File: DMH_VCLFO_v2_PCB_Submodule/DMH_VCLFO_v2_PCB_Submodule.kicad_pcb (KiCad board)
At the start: 2 copper layers, 88 x 70 mm, 3 parts, among them J41 Conn_02x03_Odd_Even, J43 Conn_02x03_Odd_Even, J45 Conn_02x03_Odd_Even

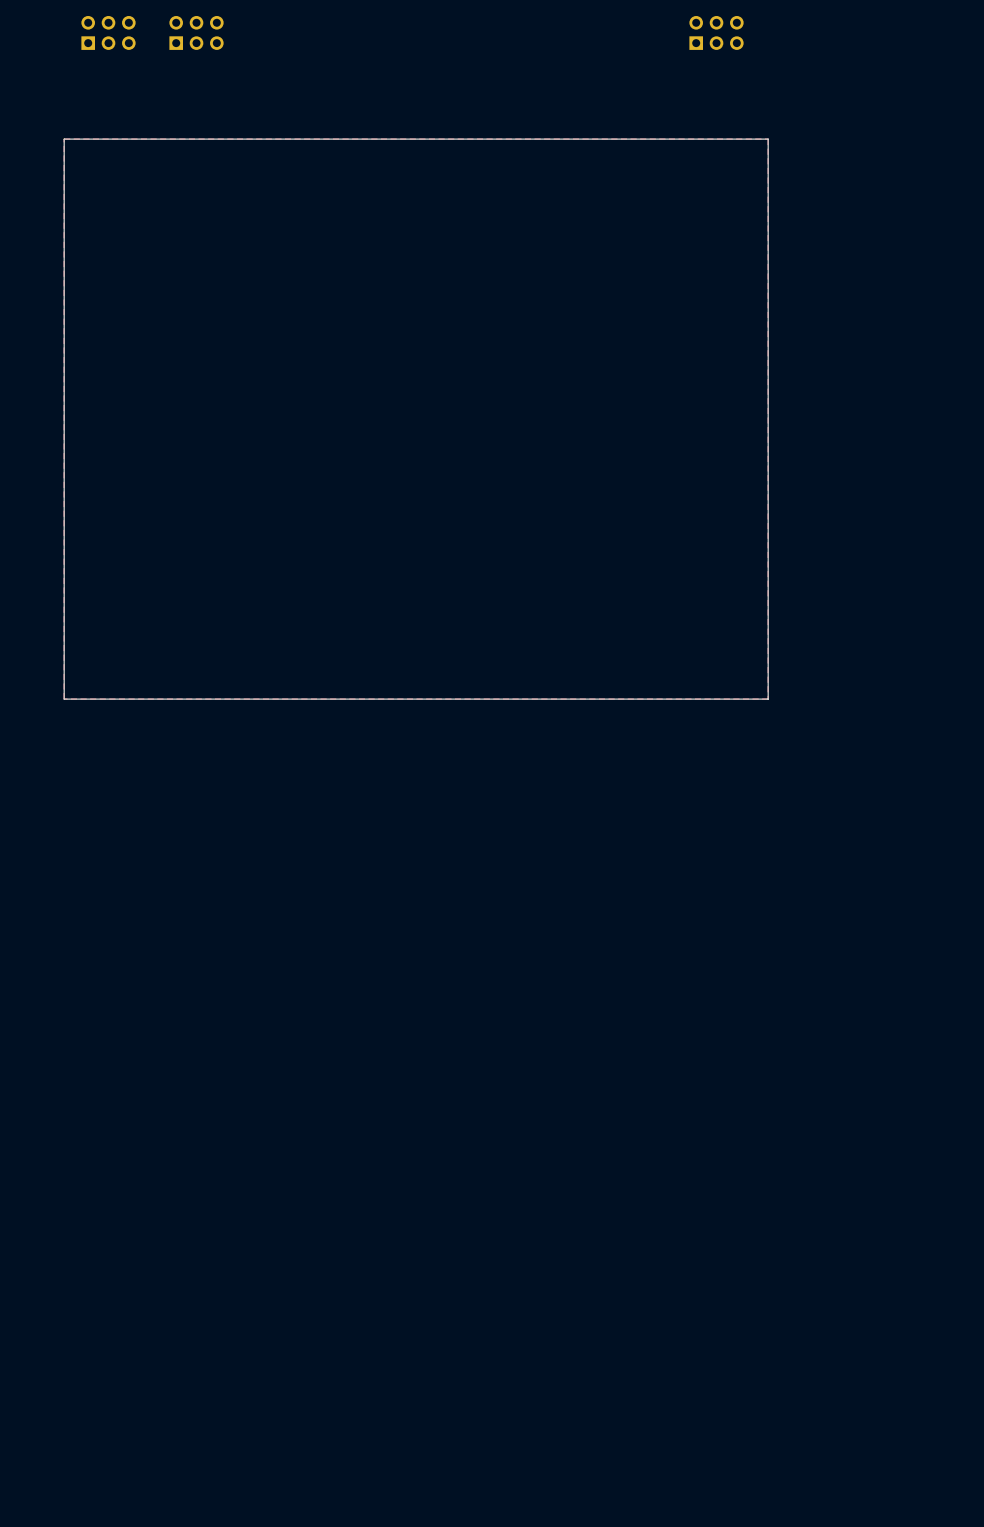
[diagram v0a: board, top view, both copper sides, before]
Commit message: Submodule comp placement started
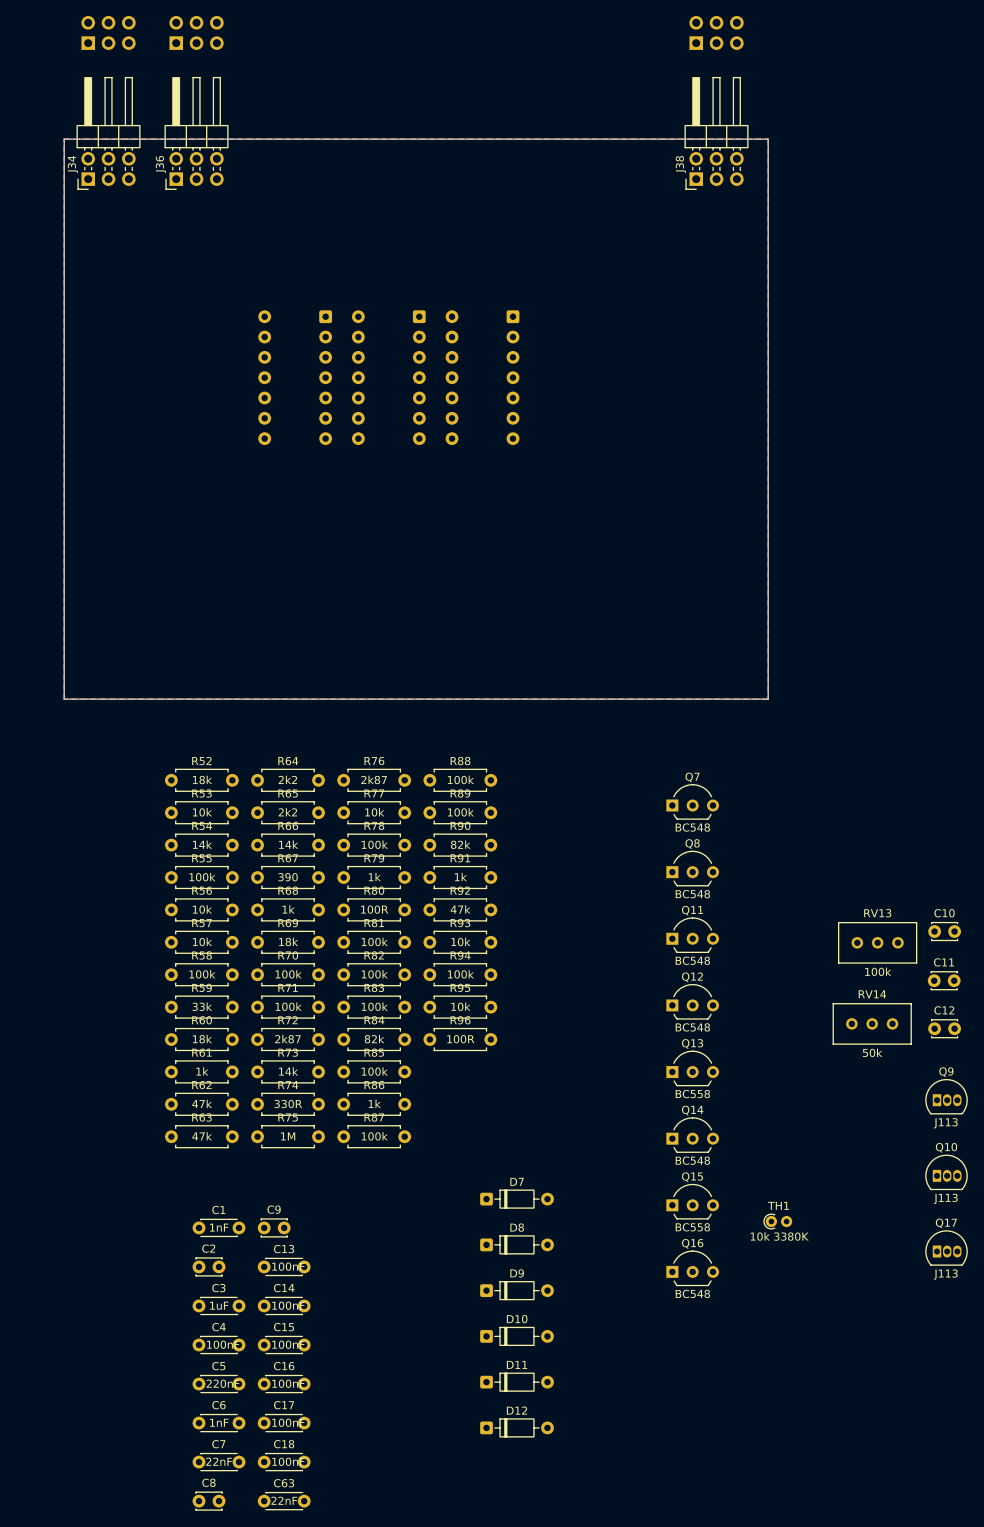
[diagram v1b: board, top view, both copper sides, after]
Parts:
- removed J41, J43, J45: Conn_02x03_Odd_Even, Connector_PinSocket_2.54mm:PinSocket_2x03_P2.54mm_Vertical
- added C1: 1nF, Capacitor_THT:C_Disc_D4.3mm_W1.9mm_P5.00mm, F.Cu at (72.8, 166.1)
- added C10: 10pF, Capacitor_THT:C_Disc_D3.0mm_W2.0mm_P2.50mm, F.Cu at (164.8, 129.1)
- added C11: 10pF, Capacitor_THT:C_Disc_D3.0mm_W2.0mm_P2.50mm, F.Cu at (164.8, 135.2)
- added C12: 100pF, Capacitor_THT:C_Disc_D3.0mm_W2.0mm_P2.50mm, F.Cu at (164.8, 141.2)
- added C13: 100nF, Capacitor_THT:C_Disc_D4.3mm_W1.9mm_P5.00mm, F.Cu at (81.0, 171.0)
- added C14: 100nF, Capacitor_THT:C_Disc_D4.3mm_W1.9mm_P5.00mm, F.Cu at (81.0, 175.9)
- added C15: 100nF, Capacitor_THT:C_Disc_D4.3mm_W1.9mm_P5.00mm, F.Cu at (81.0, 180.7)
- added C16: 100nF, Capacitor_THT:C_Disc_D4.3mm_W1.9mm_P5.00mm, F.Cu at (81.0, 185.6)
- added C17: 100nF, Capacitor_THT:C_Disc_D4.3mm_W1.9mm_P5.00mm, F.Cu at (81.0, 190.5)
- added C18: 100nF, Capacitor_THT:C_Disc_D4.3mm_W1.9mm_P5.00mm, F.Cu at (81.0, 195.4)
- added C2: 100pF, Capacitor_THT:C_Disc_D3.0mm_W2.0mm_P2.50mm, F.Cu at (72.8, 171.0)
- added C3: 1uF, Capacitor_THT:C_Disc_D4.3mm_W1.9mm_P5.00mm, F.Cu at (72.8, 175.9)
- added C4: 100nF, Capacitor_THT:C_Disc_D4.3mm_W1.9mm_P5.00mm, F.Cu at (72.8, 180.7)
- added C5: 220nF, Capacitor_THT:C_Disc_D4.3mm_W1.9mm_P5.00mm, F.Cu at (72.8, 185.6)
- added C6: 1nF, Capacitor_THT:C_Disc_D4.3mm_W1.9mm_P5.00mm, F.Cu at (72.8, 190.5)
- added C63: 22nF, Capacitor_THT:C_Disc_D4.3mm_W1.9mm_P5.00mm, F.Cu at (81.0, 200.2)
- added C7: 22nF, Capacitor_THT:C_Disc_D4.3mm_W1.9mm_P5.00mm, F.Cu at (72.8, 195.4)
- added C8: 100pF, Capacitor_THT:C_Disc_D3.0mm_W2.0mm_P2.50mm, F.Cu at (72.8, 200.2)
- added C9: 2.2nF, Capacitor_THT:C_Disc_D3.0mm_W2.0mm_P2.50mm, F.Cu at (81.0, 166.1)
- added D10: 1N4148, Diode_THT:D_DO-35_SOD27_P7.62mm_Horizontal, F.Cu at (108.8, 179.7)
- added D11: 1N4148, Diode_THT:D_DO-35_SOD27_P7.62mm_Horizontal, F.Cu at (108.8, 185.4)
- added D12: 1N4148, Diode_THT:D_DO-35_SOD27_P7.62mm_Horizontal, F.Cu at (108.8, 191.1)
- added D7: 1N4148, Diode_THT:D_DO-35_SOD27_P7.62mm_Horizontal, F.Cu at (108.8, 162.5)
- added D8: 1N4148, Diode_THT:D_DO-35_SOD27_P7.62mm_Horizontal, F.Cu at (108.8, 168.2)
- added D9: 1N4148, Diode_THT:D_DO-35_SOD27_P7.62mm_Horizontal, F.Cu at (108.8, 173.9)
- added J34: Conn_02x03_Odd_Even, Connector_PinHeader_2.54mm:PinHeader_2x03_P2.54mm_Horizontal, F.Cu at (59.0, 35.0)
- added J35: Conn_02x03_Odd_Even, Connector_PinSocket_2.54mm:PinSocket_2x03_P2.54mm_Vertical, B.Cu at (59.0, 18.0)
- added J36: Conn_02x03_Odd_Even, Connector_PinHeader_2.54mm:PinHeader_2x03_P2.54mm_Horizontal, F.Cu at (70.0, 35.0)
- added J37: Conn_02x03_Odd_Even, Connector_PinSocket_2.54mm:PinSocket_2x03_P2.54mm_Vertical, B.Cu at (70.0, 18.0)
- added J38: Conn_02x03_Odd_Even, Connector_PinHeader_2.54mm:PinHeader_2x03_P2.54mm_Horizontal, F.Cu at (135.0, 35.0)
- added J39: Conn_02x03_Odd_Even, Connector_PinSocket_2.54mm:PinSocket_2x03_P2.54mm_Vertical, B.Cu at (135.0, 18.0)
- added Q10: J113, Package_TO_SOT_THT:TO-92L_Inline, F.Cu at (165.1, 159.6)
- added Q11: BC548, Package_TO_SOT_THT:TO-92L_Inline_Wide, F.Cu at (132.0, 130.0)
- added Q12: BC548, Package_TO_SOT_THT:TO-92L_Inline_Wide, F.Cu at (132.0, 138.3)
- added Q13: BC558, Package_TO_SOT_THT:TO-92L_Inline_Wide, F.Cu at (132.0, 146.6)
- added Q14: BC548, Package_TO_SOT_THT:TO-92L_Inline_Wide, F.Cu at (132.0, 154.9)
- added Q15: BC558, Package_TO_SOT_THT:TO-92L_Inline_Wide, F.Cu at (132.0, 163.3)
- added Q16: BC548, Package_TO_SOT_THT:TO-92L_Inline_Wide, F.Cu at (132.0, 171.6)
- added Q17: J113, Package_TO_SOT_THT:TO-92L_Inline, F.Cu at (165.1, 169.1)
- added Q7: BC548, Package_TO_SOT_THT:TO-92L_Inline_Wide, F.Cu at (132.0, 113.3)
- added Q8: BC548, Package_TO_SOT_THT:TO-92L_Inline_Wide, F.Cu at (132.0, 121.6)
- added Q9: J113, Package_TO_SOT_THT:TO-92L_Inline, F.Cu at (165.1, 150.1)
- added R52: 18k, Resistor_THT:R_Axial_DIN0207_L6.3mm_D2.5mm_P7.62mm_Horizontal, F.Cu at (69.4, 110.2)
- added R53: 10k, Resistor_THT:R_Axial_DIN0207_L6.3mm_D2.5mm_P7.62mm_Horizontal, F.Cu at (69.4, 114.2)
- added R54: 14k, Resistor_THT:R_Axial_DIN0207_L6.3mm_D2.5mm_P7.62mm_Horizontal, F.Cu at (69.4, 118.2)
- added R55: 100k, Resistor_THT:R_Axial_DIN0207_L6.3mm_D2.5mm_P7.62mm_Horizontal, F.Cu at (69.4, 122.3)
- added R56: 10k, Resistor_THT:R_Axial_DIN0207_L6.3mm_D2.5mm_P7.62mm_Horizontal, F.Cu at (69.4, 126.3)
- added R57: 10k, Resistor_THT:R_Axial_DIN0207_L6.3mm_D2.5mm_P7.62mm_Horizontal, F.Cu at (69.4, 130.4)
- added R58: 100k, Resistor_THT:R_Axial_DIN0207_L6.3mm_D2.5mm_P7.62mm_Horizontal, F.Cu at (69.4, 134.4)
- added R59: 33k, Resistor_THT:R_Axial_DIN0207_L6.3mm_D2.5mm_P7.62mm_Horizontal, F.Cu at (69.4, 138.5)
- added R60: 18k, Resistor_THT:R_Axial_DIN0207_L6.3mm_D2.5mm_P7.62mm_Horizontal, F.Cu at (69.4, 142.6)
- added R61: 1k, Resistor_THT:R_Axial_DIN0207_L6.3mm_D2.5mm_P7.62mm_Horizontal, F.Cu at (69.4, 146.6)
- added R62: 47k, Resistor_THT:R_Axial_DIN0207_L6.3mm_D2.5mm_P7.62mm_Horizontal, F.Cu at (69.4, 150.7)
- added R63: 47k, Resistor_THT:R_Axial_DIN0207_L6.3mm_D2.5mm_P7.62mm_Horizontal, F.Cu at (69.4, 154.7)
- added R64: 2k2, Resistor_THT:R_Axial_DIN0207_L6.3mm_D2.5mm_P7.62mm_Horizontal, F.Cu at (80.2, 110.2)
- added R65: 2k2, Resistor_THT:R_Axial_DIN0207_L6.3mm_D2.5mm_P7.62mm_Horizontal, F.Cu at (80.2, 114.2)
- added R66: 14k, Resistor_THT:R_Axial_DIN0207_L6.3mm_D2.5mm_P7.62mm_Horizontal, F.Cu at (80.2, 118.2)
- added R67: 390, Resistor_THT:R_Axial_DIN0207_L6.3mm_D2.5mm_P7.62mm_Horizontal, F.Cu at (80.2, 122.3)
- added R68: 1k, Resistor_THT:R_Axial_DIN0207_L6.3mm_D2.5mm_P7.62mm_Horizontal, F.Cu at (80.2, 126.3)
- added R69: 18k, Resistor_THT:R_Axial_DIN0207_L6.3mm_D2.5mm_P7.62mm_Horizontal, F.Cu at (80.2, 130.4)
- added R70: 100k, Resistor_THT:R_Axial_DIN0207_L6.3mm_D2.5mm_P7.62mm_Horizontal, F.Cu at (80.2, 134.4)
- added R71: 100k, Resistor_THT:R_Axial_DIN0207_L6.3mm_D2.5mm_P7.62mm_Horizontal, F.Cu at (80.2, 138.5)
- added R72: 2k87, Resistor_THT:R_Axial_DIN0207_L6.3mm_D2.5mm_P7.62mm_Horizontal, F.Cu at (80.2, 142.6)
- added R73: 14k, Resistor_THT:R_Axial_DIN0207_L6.3mm_D2.5mm_P7.62mm_Horizontal, F.Cu at (80.2, 146.6)
- added R74: 330R, Resistor_THT:R_Axial_DIN0207_L6.3mm_D2.5mm_P7.62mm_Horizontal, F.Cu at (80.2, 150.7)
- added R75: 1M, Resistor_THT:R_Axial_DIN0207_L6.3mm_D2.5mm_P7.62mm_Horizontal, F.Cu at (80.2, 154.7)
- added R76: 2k87, Resistor_THT:R_Axial_DIN0207_L6.3mm_D2.5mm_P7.62mm_Horizontal, F.Cu at (90.9, 110.2)
- added R77: 10k, Resistor_THT:R_Axial_DIN0207_L6.3mm_D2.5mm_P7.62mm_Horizontal, F.Cu at (90.9, 114.2)
- added R78: 100k, Resistor_THT:R_Axial_DIN0207_L6.3mm_D2.5mm_P7.62mm_Horizontal, F.Cu at (90.9, 118.2)
- added R79: 1k, Resistor_THT:R_Axial_DIN0207_L6.3mm_D2.5mm_P7.62mm_Horizontal, F.Cu at (90.9, 122.3)
- added R80: 100R, Resistor_THT:R_Axial_DIN0207_L6.3mm_D2.5mm_P7.62mm_Horizontal, F.Cu at (90.9, 126.3)
- added R81: 100k, Resistor_THT:R_Axial_DIN0207_L6.3mm_D2.5mm_P7.62mm_Horizontal, F.Cu at (90.9, 130.4)
- added R82: 100k, Resistor_THT:R_Axial_DIN0207_L6.3mm_D2.5mm_P7.62mm_Horizontal, F.Cu at (90.9, 134.4)
- added R83: 100k, Resistor_THT:R_Axial_DIN0207_L6.3mm_D2.5mm_P7.62mm_Horizontal, F.Cu at (90.9, 138.5)
- added R84: 82k, Resistor_THT:R_Axial_DIN0207_L6.3mm_D2.5mm_P7.62mm_Horizontal, F.Cu at (90.9, 142.6)
- added R85: 100k, Resistor_THT:R_Axial_DIN0207_L6.3mm_D2.5mm_P7.62mm_Horizontal, F.Cu at (90.9, 146.6)
- added R86: 1k, Resistor_THT:R_Axial_DIN0207_L6.3mm_D2.5mm_P7.62mm_Horizontal, F.Cu at (90.9, 150.7)
- added R87: 100k, Resistor_THT:R_Axial_DIN0207_L6.3mm_D2.5mm_P7.62mm_Horizontal, F.Cu at (90.9, 154.7)
- added R88: 100k, Resistor_THT:R_Axial_DIN0207_L6.3mm_D2.5mm_P7.62mm_Horizontal, F.Cu at (101.7, 110.2)
- added R89: 100k, Resistor_THT:R_Axial_DIN0207_L6.3mm_D2.5mm_P7.62mm_Horizontal, F.Cu at (101.7, 114.2)
- added R90: 82k, Resistor_THT:R_Axial_DIN0207_L6.3mm_D2.5mm_P7.62mm_Horizontal, F.Cu at (101.7, 118.2)
- added R91: 1k, Resistor_THT:R_Axial_DIN0207_L6.3mm_D2.5mm_P7.62mm_Horizontal, F.Cu at (101.7, 122.3)
- added R92: 47k, Resistor_THT:R_Axial_DIN0207_L6.3mm_D2.5mm_P7.62mm_Horizontal, F.Cu at (101.7, 126.3)
- added R93: 10k, Resistor_THT:R_Axial_DIN0207_L6.3mm_D2.5mm_P7.62mm_Horizontal, F.Cu at (101.7, 130.4)
- added R94: 100k, Resistor_THT:R_Axial_DIN0207_L6.3mm_D2.5mm_P7.62mm_Horizontal, F.Cu at (101.7, 134.4)
- added R95: 10k, Resistor_THT:R_Axial_DIN0207_L6.3mm_D2.5mm_P7.62mm_Horizontal, F.Cu at (101.7, 138.5)
- added R96: 100R, Resistor_THT:R_Axial_DIN0207_L6.3mm_D2.5mm_P7.62mm_Horizontal, F.Cu at (101.7, 142.6)
- added RV13: 100k, Potentiometer_THT:Potentiometer_Bourns_3296W_Vertical, F.Cu at (160.2, 130.5)
- added RV14: 50k, Potentiometer_THT:Potentiometer_Bourns_3296W_Vertical, F.Cu at (159.5, 140.6)
- added TH1: 10k 3380K, Resistor_THT:R_Axial_DIN0204_L3.6mm_D1.6mm_P1.90mm_Vertical, F.Cu at (144.4, 165.3)
- added U10: TL074, Package_DIP:DIP-14_W7.62mm_Socket, B.Cu at (88.7, 52.2)
- added U11: TL074, Package_DIP:DIP-14_W7.62mm_Socket, B.Cu at (100.4, 52.2)
- added U12: TL074, Package_DIP:DIP-14_W7.62mm_Socket, B.Cu at (112.1, 52.2)

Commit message: Submodule com placement done
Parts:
- removed J35, J37, J39: Conn_02x03_Odd_Even, Connector_PinSocket_2.54mm:PinSocket_2x03_P2.54mm_Vertical
- C1, C10, C11, C12, C13, C14, C15, C16, C17, C18, C2, C3, C4, C5, C6, C63, C7, C8, C9, D10, D11, D12, D7, D8, D9, Q10, Q11, Q12, Q13, Q14, Q15, Q16, Q17, Q7, Q8, Q9, R52, R53, R54, R55, R56, R57, R58, R59, R60, R61, R62, R63, R64, R65, R66, R67, R68, R69, R70, R71, R72, R73, R74, R75, R76, R77, R78, R79, R80, R81, R82, R83, R84, R85, R86, R87, R88, R89, R90, R91, R92, R93, R94, R95, R96, RV13, RV14: moved to B.Cu
- TH1: value 10k 3380K -> 10k3380; moved to B.Cu
- moved Q10 160.3 mm to (56.3, 41.9)
- moved C63 158.2 mm to (65.6, 42.8)
- moved C7 149.4 mm to (65.6, 46.1)
- moved C5 146.3 mm to (65.6, 39.5)
- moved D12 139.4 mm to (93.2, 52.6), turned to 180 degrees
- moved C6 138.2 mm to (123.9, 62.1), turned to 180 degrees
- moved C15 137.0 mm to (129.4, 52.6)
- moved C1 134.5 mm to (97.5, 33.9)
- moved C2 134.3 mm to (111.8, 42.5)
- moved Q17 130.0 mm to (78.7, 71.9), turned to -90 degrees
- moved TH1 129.9 mm to (54.5, 71.5), turned to 180 degrees
- moved C18 128.3 mm to (129.5, 76.6)
- moved C8 124.8 mm to (92.3, 77.0)
- moved C14 124.4 mm to (97.5, 52.6)
- moved C4 124.1 mm to (146.8, 81.1), turned to 90 degrees
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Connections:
- C3 pad 2: Net-(U12A-+) -> Net-(U12D-+)
- C6 pad 1: Net-(U12D-+) -> Net-(U12A-+)
- R71 pad 2: Net-(U12A--) -> Net-(U12D--)
- R73 pad 1: Net-(U12A-+) -> Net-(U12D-+)
- R74 pad 1: Net-(U12A--) -> Net-(U12D--)
- R78 pad 1: Net-(U12D-+) -> Net-(U12A-+)
- U12 pad 1: Net-(Q9-D) -> Net-(D10-K)
- U12 pad 10: Net-(Q8-C) -> Net-(Q9-S)
- U12 pad 13: /SubModule A/Comp_Ref -> Net-(U12D--)
- U12 pad 14: Net-(D10-K) -> Net-(Q9-D)
- U12 pad 2: Net-(U12A--) -> /SubModule A/Comp_Ref
- U12 pad 5: Net-(Q9-S) -> Net-(Q8-C)
- U12 pad 6: A_Rnd_S -> Net-(Q7-C)
- U12 pad 7: A_Rnd_S -> Net-(R54-Pad2)
- U12 pad 8: Net-(R54-Pad2) -> A_Rnd_S
- U12 pad 9: Net-(Q7-C) -> A_Rnd_S
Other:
- board size 88 x 70 mm -> 100 x 70 mm

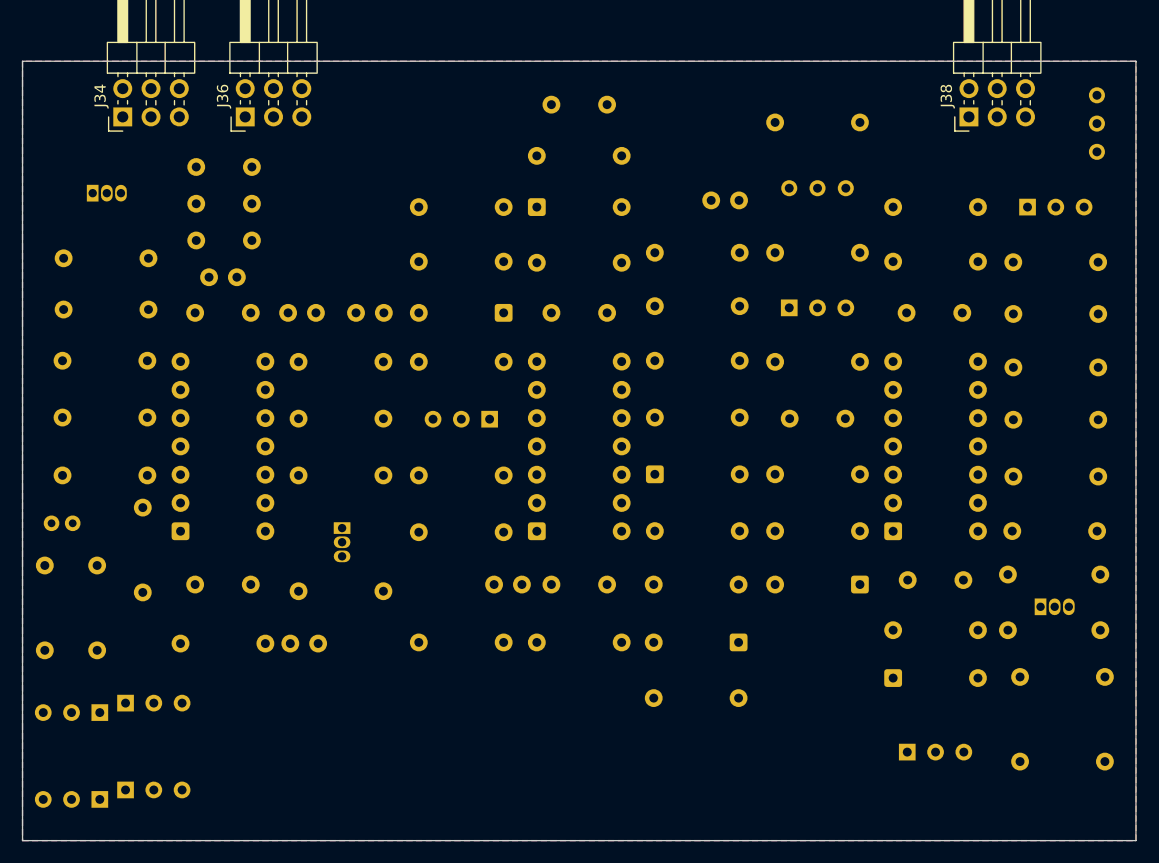
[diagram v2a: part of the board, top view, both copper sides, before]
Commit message: Submodule routing done
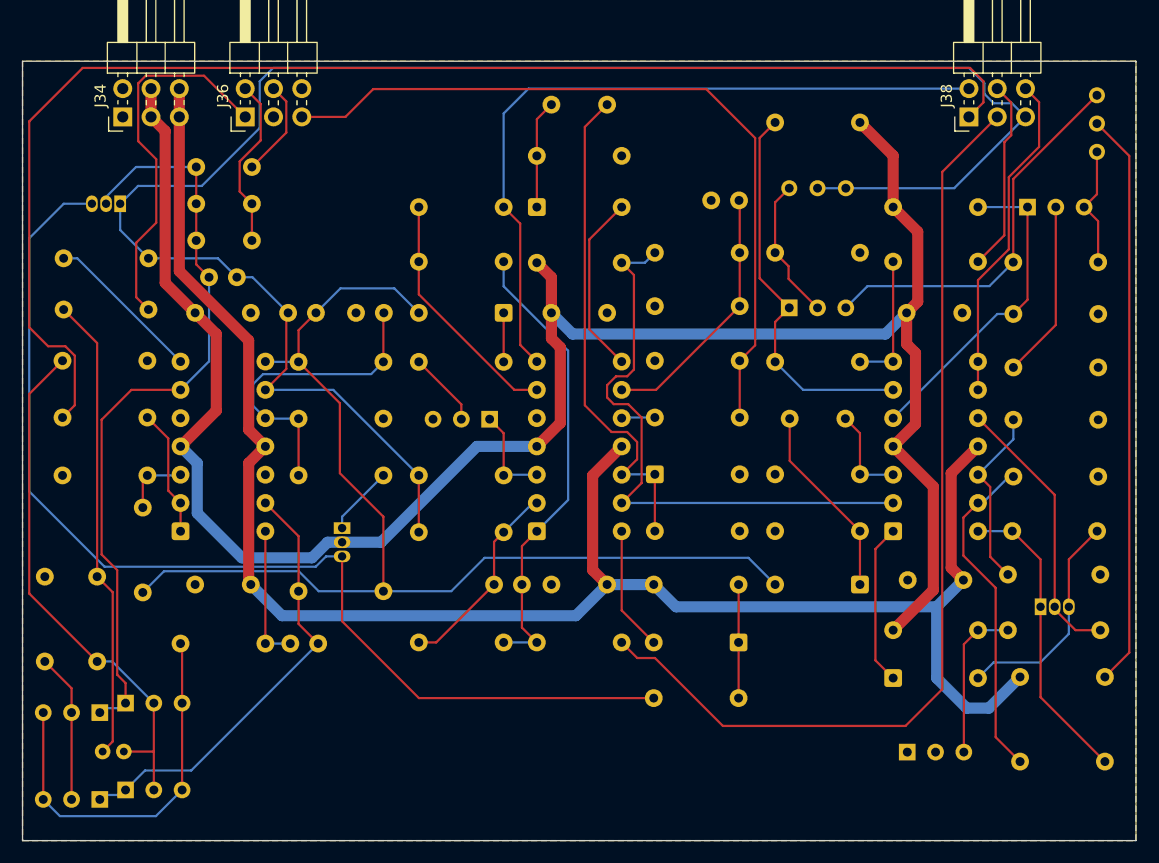
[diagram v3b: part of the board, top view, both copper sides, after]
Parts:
- moved TH1 20.7 mm to (57.2, 92.0), turned to 0 degrees
- moved Q10 2.65 mm to (58.8, 42.8), turned to 180 degrees
- moved R76 1.00 mm to (56.7, 76.3)
- moved R96 1.00 mm to (52.0, 83.9)
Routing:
- net +12V: track 0.00 -> 182.8 mm
- net A_Tri_S: track 0.00 -> 162.9 mm
- net -12V: track 0.00 -> 160.2 mm
- net A_Sqr_S: track 0.00 -> 121.6 mm
- net /SubModule A/Sqr_Raw: track 0.00 -> 103.4 mm
- net /SubModule A/Reset_pulse: track 0.00 -> 97.6 mm
- net A_Saw_S: track 0.00 -> 86.7 mm
- net A_Sync_S: track 0.00 -> 69.3 mm
- net Net-(Q10-S): track 0.00 -> 68.6 mm
- net A_Rmp_S: track 0.00 -> 66.2 mm
- net /SubModule A/Comp_Ref: track 0.00 -> 54.1 mm
- net Net-(R69-Pad2): track 0.00 -> 51.8 mm
- net Net-(Q12-B): track 0.00 -> 47.9 mm
- net Net-(D9-K): track 0.00 -> 45.5 mm
- net Net-(R72-Pad2): track 0.00 -> 41.9 mm
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
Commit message: Generated Gerbers
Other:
- board text added: "Mk1.0 - March 2026"
- board text removed: "Mk1.0 - Month Year"
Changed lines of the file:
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@@
 			(plot_on_all_layers_selection 0x00000000_00000000_00000000_00000000)
 			(disableapertmacros no)
-			(usegerberextensions no)
+			(usegerberextensions yes)
 			(usegerberattributes yes)
 			(usegerberadvancedattributes yes)
@@
 			(sketchdnponfab yes)
 			(crossoutdnponfab yes)
-			(subtractmaskfromsilk no)
+			(subtractmaskfromsilk yes)
 			(outputformat 1)
 			(mirror no)
-			(drillshape 1)
+			(drillshape 0)
 			(scaleselection 1)
-			(outputdirectory "")
+			(outputdirectory "Gerbers/")
 		)
 	)
@@
 		(layer "Edge.Cuts")
 	)
-	(gr_text "Mk1.0 - Month Year"
+	(gr_text "Mk1.0 - March 2026"
 		(at 100 98.5 0)
 		(layer "B.SilkS")
